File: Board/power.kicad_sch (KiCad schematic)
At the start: 6 parts, among them J1 Conn_01x02, U1 OKI-78SR-3.3_1.5-W36H-C

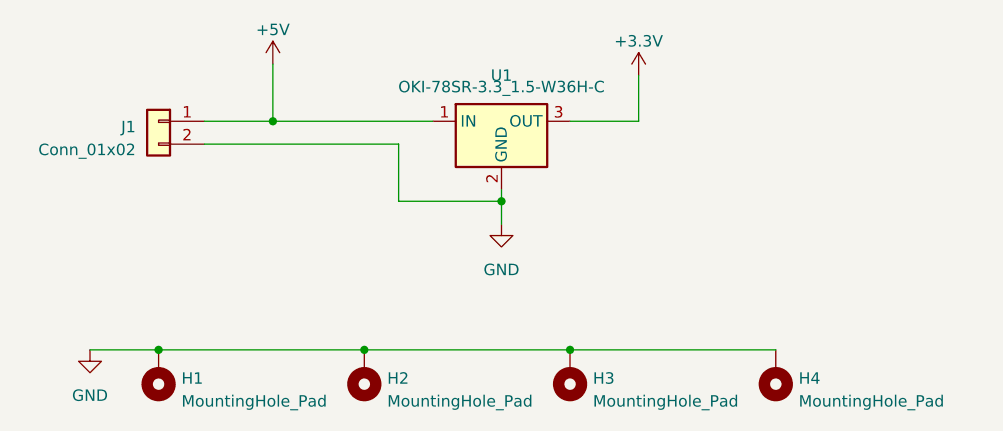
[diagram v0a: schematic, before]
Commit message: fix 3.3v regulator footprint
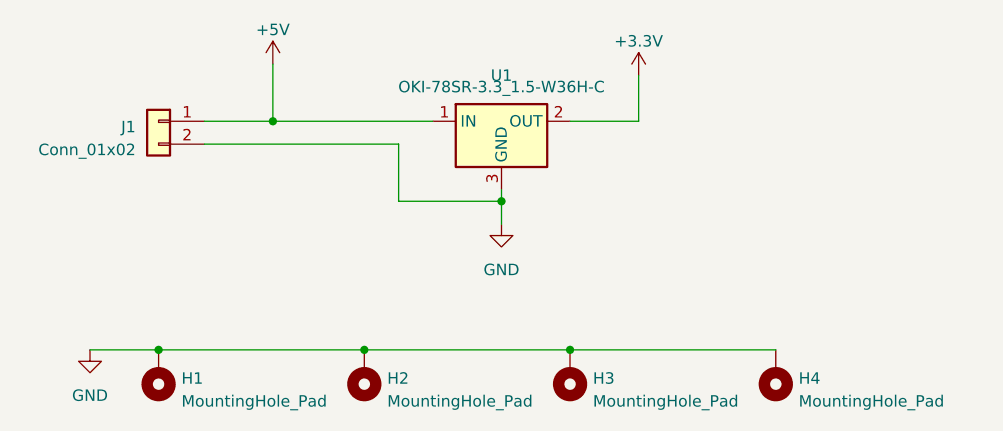
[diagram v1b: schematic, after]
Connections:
- net +3.3V: now also U1.2 (OUT); no longer U1.3 (OUT)
- net GND: now also U1.3 (GND); no longer U1.2 (GND)
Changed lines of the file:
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@@
     )
     (pin "1")
+    (pin "3")
     (pin "2")
-    (pin "3")
     (instances
       (project "binary_clock"
